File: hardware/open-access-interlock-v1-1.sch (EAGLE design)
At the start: 20 parts

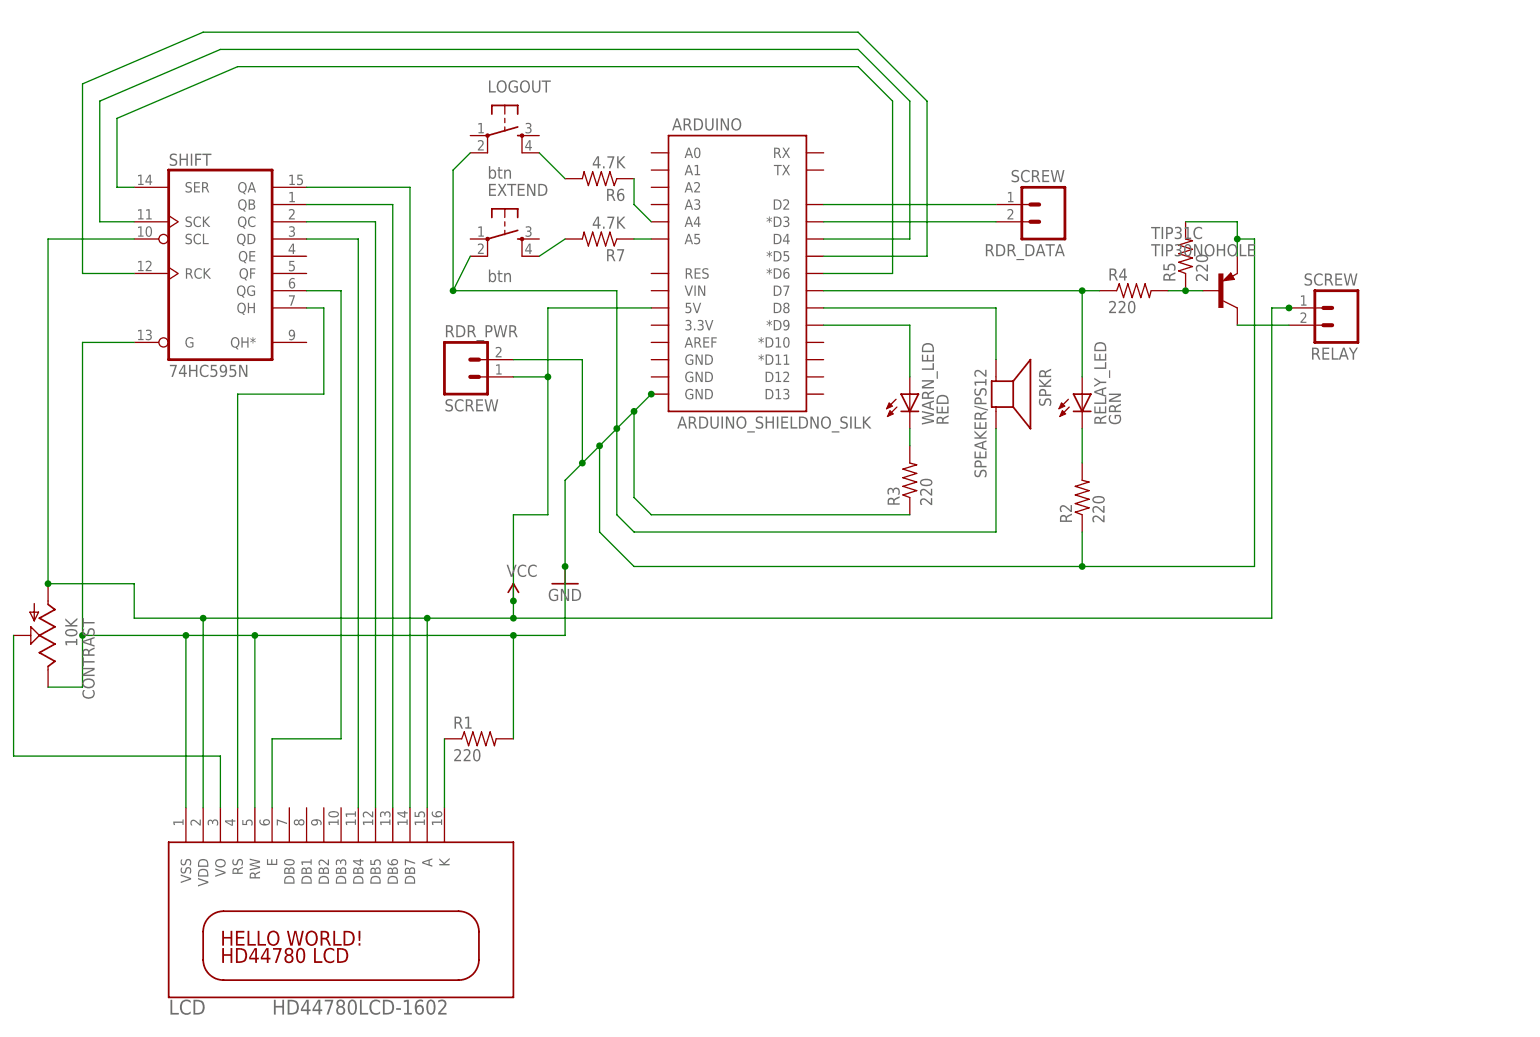
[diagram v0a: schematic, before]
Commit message: Updated with better screw terminals
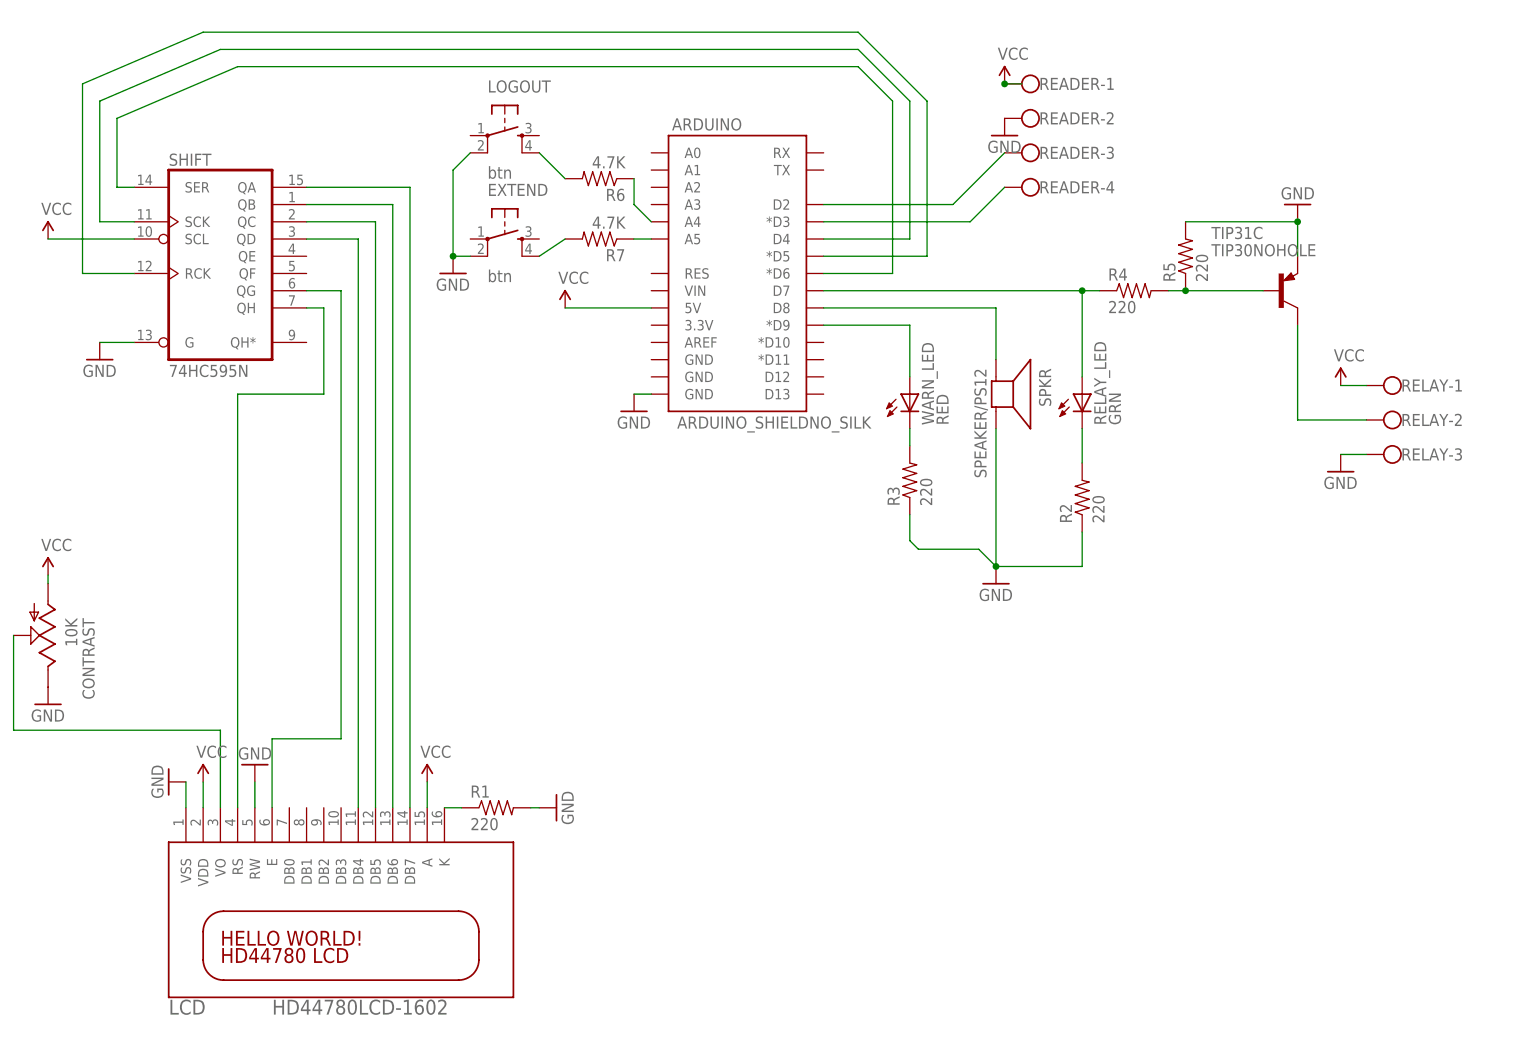
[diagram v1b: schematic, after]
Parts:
- removed RDR_DATA, RDR_PWR: SCREW, SparkFun:M023.5MM
- added READER: (no value), con-wago-500:W237-4
- RELAY: value SCREW -> (none); device SparkFun:M023.5MM -> con-wago-500:W237-103
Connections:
- net GND: now also READER-2.KL, RELAY-3.KL; no longer RDR_PWR.2
- net N$1: now also READER-3.KL; no longer RDR_DATA.1
- net N$13: now also RELAY-2.KL; no longer RELAY.2
- net N$2: now also READER-4.KL; no longer RDR_DATA.2
- net VCC: now also READER-1.KL, RELAY-1.KL; no longer RDR_PWR.1, RELAY.1
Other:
- moved on the sheet: R1, TIP31C

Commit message: Final tweaks for terminals and labels
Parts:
- READER: device con-wago-500:W237-4 -> SparkFun-Connectors:M04SCREW
- RELAY: device con-wago-500:W237-103 -> SparkFun-Connectors:M03SCREW
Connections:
- net GND: now also READER.2, RELAY.3; no longer READER-2.KL, RELAY-3.KL
- net N$1: now also READER.3; no longer READER-3.KL
- net N$13: now also RELAY.2; no longer RELAY-2.KL
- net N$2: now also READER.4; no longer READER-4.KL
- net VCC: now also READER.1, RELAY.1; no longer READER-1.KL, RELAY-1.KL
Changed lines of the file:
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@@
 <part name="GND9" library="SparkFun" deviceset="GND" device=""/>
 <part name="GND10" library="SparkFun" deviceset="GND" device=""/>
-<part name="RELAY" library="con-wago-500" deviceset="W237-103" device=""/>
-<part name="READER" library="con-wago-500" deviceset="W237-4" device=""/>
 <part name="GND11" library="SparkFun" deviceset="GND" device=""/>
 <part name="P+3" library="SparkFun" deviceset="VCC" device=""/>
@@
 <part name="P+7" library="SparkFun" deviceset="VCC" device=""/>
 <part name="P+8" library="SparkFun" deviceset="VCC" device=""/>
+<part name="RELAY" library="SparkFun-Connectors" deviceset="M03" device="SCREW"/>
+<part name="READER" library="SparkFun-Connectors" deviceset="M04" device="SCREW"/>
 </parts>
 <sheets>
@@
 <instance part="R6" gate="G$1" x="38.1" y="52.07" rot="R180"/>
 <instance part="R7" gate="G$1" x="38.1" y="43.18" rot="R180"/>
-<instance part="P+2" gate="1" x="97.79" y="66.04"/>
-<instance part="GND2" gate="1" x="97.79" y="58.42"/>
+<instance part="P+2" gate="1" x="90.17" y="60.96"/>
+<instance part="GND2" gate="1" x="90.17" y="55.88"/>
 <instance part="GND3" gate="1" x="43.18" y="17.78"/>
 <instance part="GND5" gate="1" x="31.75" y="-40.64" rot="R90"/>
@@
 <instance part="GND9" gate="1" x="16.51" y="38.1"/>
 <instance part="GND10" gate="1" x="140.97" y="48.26" rot="R180"/>
-<instance part="RELAY" gate="-1" x="156.21" y="21.59" smashed="yes" rot="R180">
-<attribute name="NAME" x="156.21" y="20.701" size="1.778" layer="95"/>
-</instance>
-<instance part="RELAY" gate="-2" x="156.21" y="16.51" smashed="yes" rot="R180">
-<attribute name="NAME" x="156.21" y="15.621" size="1.778" layer="95"/>
-</instance>
-<instance part="RELAY" gate="-3" x="156.21" y="11.43" smashed="yes" rot="R180">
-<attribute name="VALUE" x="158.75" y="15.113" size="1.778" layer="96" rot="R180"/>
-<attribute name="NAME" x="156.21" y="10.541" size="1.778" layer="95"/>
-</instance>
-<instance part="READER" gate="-1" x="102.87" y="66.04" rot="R180"/>
-<instance part="READER" gate="-2" x="102.87" y="60.96" rot="R180"/>
-<instance part="READER" gate="-3" x="102.87" y="55.88" rot="R180"/>
-<instance part="READER" gate="-4" x="102.87" y="50.8" rot="R180"/>
-<instance part="GND11" gate="1" x="147.32" y="8.89"/>
-<instance part="P+3" gate="1" x="147.32" y="21.59"/>
+<instance part="GND11" gate="1" x="147.32" y="11.43"/>
+<instance part="P+3" gate="1" x="147.32" y="19.05"/>
 <instance part="P+4" gate="1" x="-20.32" y="-36.83"/>
 <instance part="P+5" gate="1" x="-43.18" y="-6.35"/>
@@
 <instance part="P+7" gate="1" x="12.7" y="-36.83"/>
 <instance part="P+8" gate="1" x="33.02" y="33.02"/>
+<instance part="RELAY" gate="G$1" x="158.75" y="16.51" rot="R180"/>
+<instance part="READER" gate="G$1" x="105.41" y="58.42" rot="R180"/>
 </instances>
 <busses>
@@
 <wire x1="71.12" y1="48.26" x2="90.17" y2="48.26" width="0.1524" layer="91"/>
 <pinref part="ARDUINO" gate="G$1" pin="D2"/>
-<pinref part="READER" gate="-3" pin="KL"/>
 <wire x1="90.17" y1="48.26" x2="97.79" y2="55.88" width="0.1524" layer="91"/>
+<pinref part="READER" gate="G$1" pin="3"/>
+<wire x1="97.79" y1="55.88" x2="100.33" y2="55.88" width="0.1524" layer="91"/>
 </segment>
 </net>
@@
 <wire x1="71.12" y1="45.72" x2="92.71" y2="45.72" width="0.1524" layer="91"/>
 <pinref part="ARDUINO" gate="G$1" pin="*D3"/>
-<pinref part="READER" gate="-4" pin="KL"/>
-<wire x1="92.71" y1="45.72" x2="97.79" y2="50.8" width="0.1524" layer="91"/>
+<wire x1="92.71" y1="45.72" x2="100.33" y2="53.34" width="0.1524" layer="91"/>
+<pinref part="READER" gate="G$1" pin="4"/>
 </segment>
 </net>
@@
 <net name="VCC" class="0">
 <segment>
-<pinref part="RELAY" gate="-1" pin="KL"/>
-<wire x1="147.32" y1="21.59" x2="151.13" y2="21.59" width="0.1524" layer="91"/>
-<pinref part="P+3" gate="1" pin="VCC"/>
-</segment>
-<segment>
 <pinref part="LCD" gate="G$1" pin="A"/>
 <wire x1="12.7" y1="-40.64" x2="12.7" y2="-36.83" width="0.1524" layer="91"/>
@@
 </segment>
 <segment>
-<pinref part="READER" gate="-1" pin="KL"/>
-<wire x1="100.33" y1="66.04" x2="97.79" y2="66.04" width="0.1524" layer="91"/>
+<wire x1="100.33" y1="60.96" x2="90.17" y2="60.96" width="0.1524" layer="91"/>
 <pinref part="P+2" gate="1" pin="VCC"/>
-<junction x="97.79" y="66.04"/>
+<pinref part="READER" gate="G$1" pin="1"/>
+</segment>
+<segment>
+<pinref part="P+3" gate="1" pin="VCC"/>
+<pinref part="RELAY" gate="G$1" pin="1"/>
+<wire x1="147.32" y1="19.05" x2="151.13" y2="19.05" width="0.1524" layer="91"/>
 </segment>
 </net>
@@
 <pinref part="LCD" gate="G$1" pin="RW"/>
 <wire x1="-12.7" y1="-40.64" x2="-12.7" y2="-36.83" width="0.1524" layer="91"/>
-</segment>
-<segment>
-<pinref part="GND2" gate="1" pin="GND"/>
-<pinref part="READER" gate="-2" pin="KL"/>
 </segment>
 <segment>
@@
 </segment>
 <segment>
-<pinref part="GND11" gate="1" pin="GND"/>
-<pinref part="RELAY" gate="-3" pin="KL"/>
-<wire x1="147.32" y1="11.43" x2="151.13" y2="11.43" width="0.1524" layer="91"/>
-</segment>
-<segment>
 <pinref part="GND7" gate="1" pin="GND"/>
 <pinref part="LCD" gate="G$1" pin="VSS"/>
@@
 <pinref part="GND5" gate="1" pin="GND"/>
 <wire x1="27.94" y1="-40.64" x2="29.21" y2="-40.64" width="0.1524" layer="91"/>
+</segment>
+<segment>
+<pinref part="GND2" gate="1" pin="GND"/>
+<pinref part="READER" gate="G$1" pin="2"/>
+<wire x1="90.17" y1="58.42" x2="100.33" y2="58.42" width="0.1524" layer="91"/>
+</segment>
+<segment>
+<pinref part="GND11" gate="1" pin="GND"/>
+<pinref part="RELAY" gate="G$1" pin="3"/>
+<wire x1="147.32" y1="13.97" x2="151.13" y2="13.97" width="0.1524" layer="91"/>
 </segment>
 </net>
@@
 <pinref part="TIP31C" gate="G$1" pin="C"/>
 <wire x1="140.97" y1="30.48" x2="140.97" y2="16.51" width="0.1524" layer="91"/>
-<pinref part="RELAY" gate="-2" pin="KL"/>
 <wire x1="140.97" y1="16.51" x2="151.13" y2="16.51" width="0.1524" layer="91"/>
-</segment>
-</net>
+<pinref part="RELAY" gate="G$1" pin="2"/>
+</segment>
+</net>

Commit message: Fixing transistor/relay stuff
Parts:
- removed TIP31C: TIP30NOHOLE, adafruit:TIP30NOHOLE
- added T1: TIP31, transistor:TIP31
- R4: value 220 -> 650ohm
- R5: value 220 -> 6.5K
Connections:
- new net V+: RELAY.1
- new net V-: T1.E
- net GND: no longer RELAY.3, TIP31C.E
- net N$13: now also T1.C; no longer TIP31C.C
- net N$21: now also T1.B; no longer TIP31C.B
- net VCC: no longer RELAY.1
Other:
- moved on the sheet: R5, RELAY

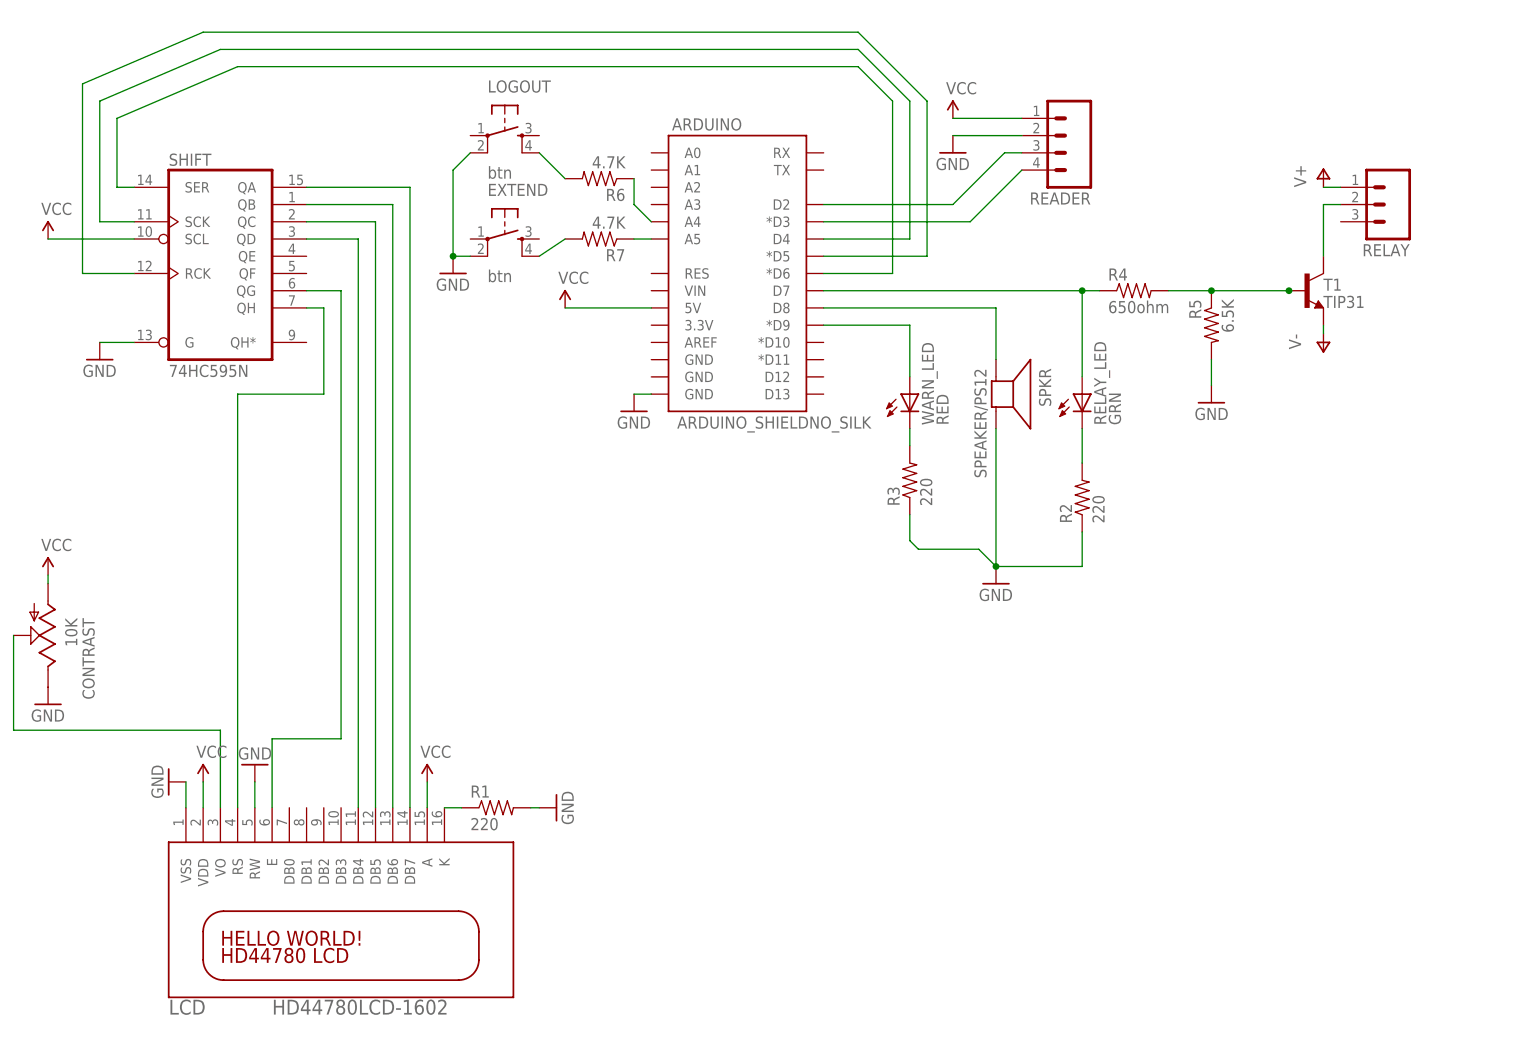
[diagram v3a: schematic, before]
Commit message: Ripping up terminal blocks
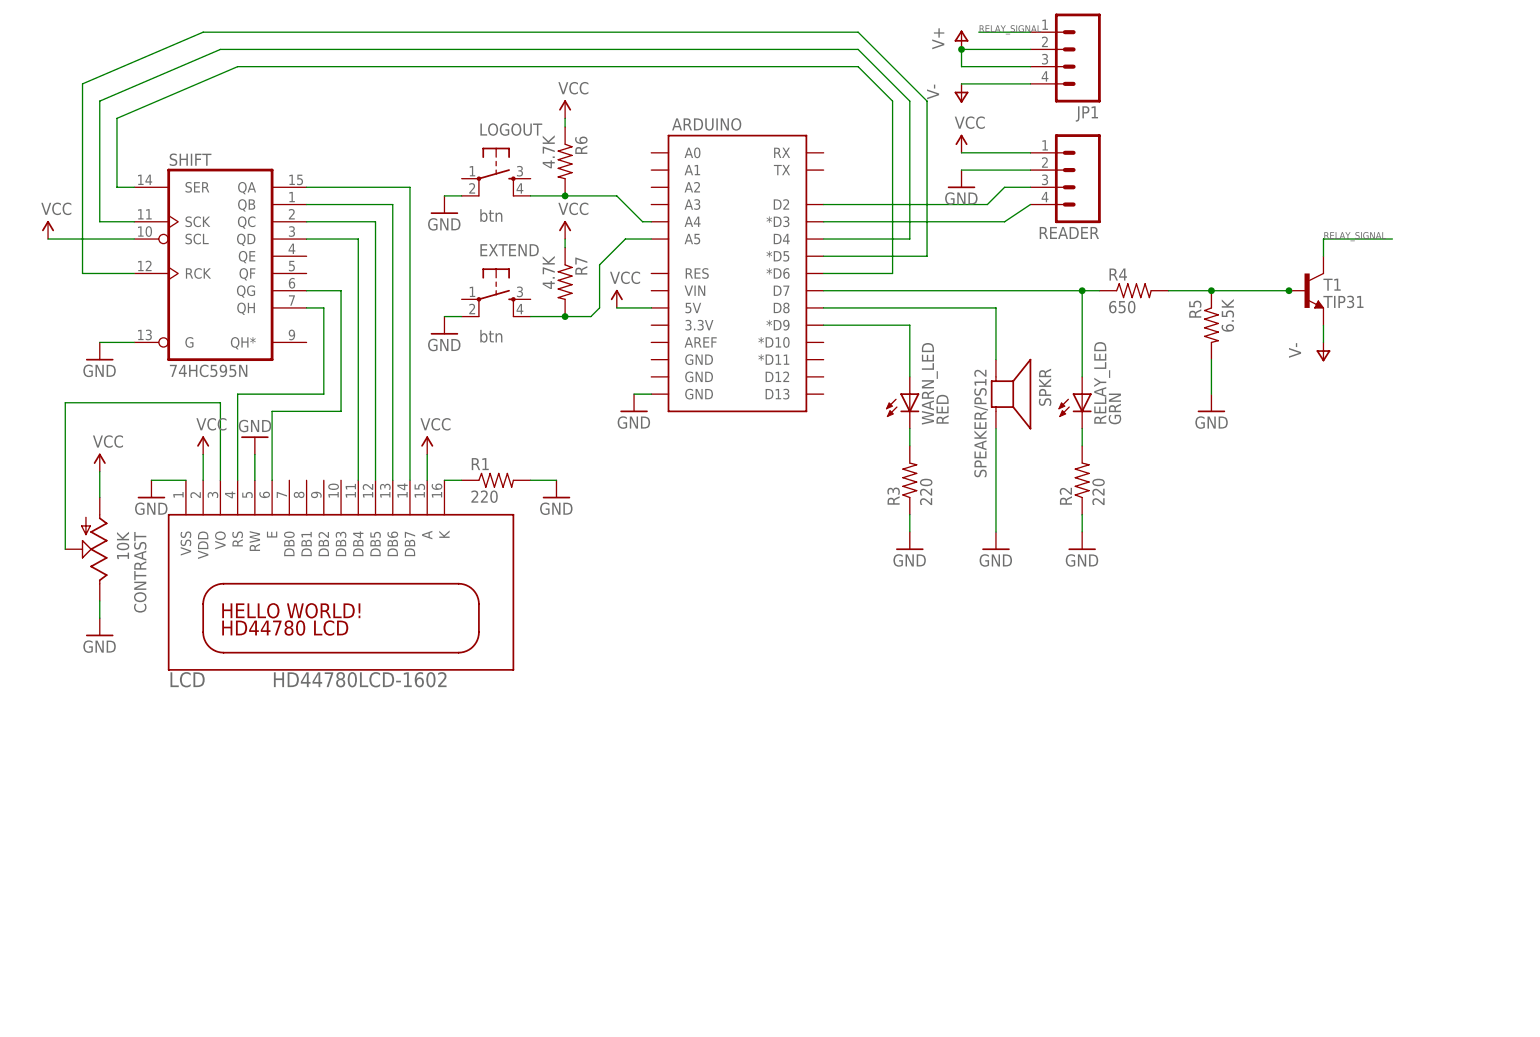
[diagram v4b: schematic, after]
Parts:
- removed RELAY: (no value), SparkFun-Connectors:M03SCREW
- added JP1: (no value), SparkFun-Connectors:M04SCREW
- R4: value 650ohm -> 650
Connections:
- removed net N$13: RELAY.2, T1.C
- removed net N$23: ARDUINO.A4, R6.1
- removed net N$24: ARDUINO.A5, R7.1
- new net RELAY_SIGNAL: JP1.1, T1.C
- net N$14: now also ARDUINO.A4
- net N$15: now also ARDUINO.A5
- net V+: now also JP1.2, JP1.3; no longer RELAY.1
- net V-: now also JP1.4
- net VCC: now also R6.1, R7.1
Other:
- moved on the sheet: CONTRAST, EXTEND, LCD, LOGOUT, R1, R2, R6, R7, READER
